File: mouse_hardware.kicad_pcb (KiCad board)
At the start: 4 copper layers, 51 x 82 mm, 48 parts, among them IC1 ADP150AUJZ-2.0-R7, IC2 AP2112K-3.3TRG1, J1 Conn_01x04_Pin, J2 Conn_01x04_Pin, SW1 SW_Push, SW5 SW_Push, U1 STM32F103RETx, U2 PMW3360DM-T2QU, Y1 8MHz

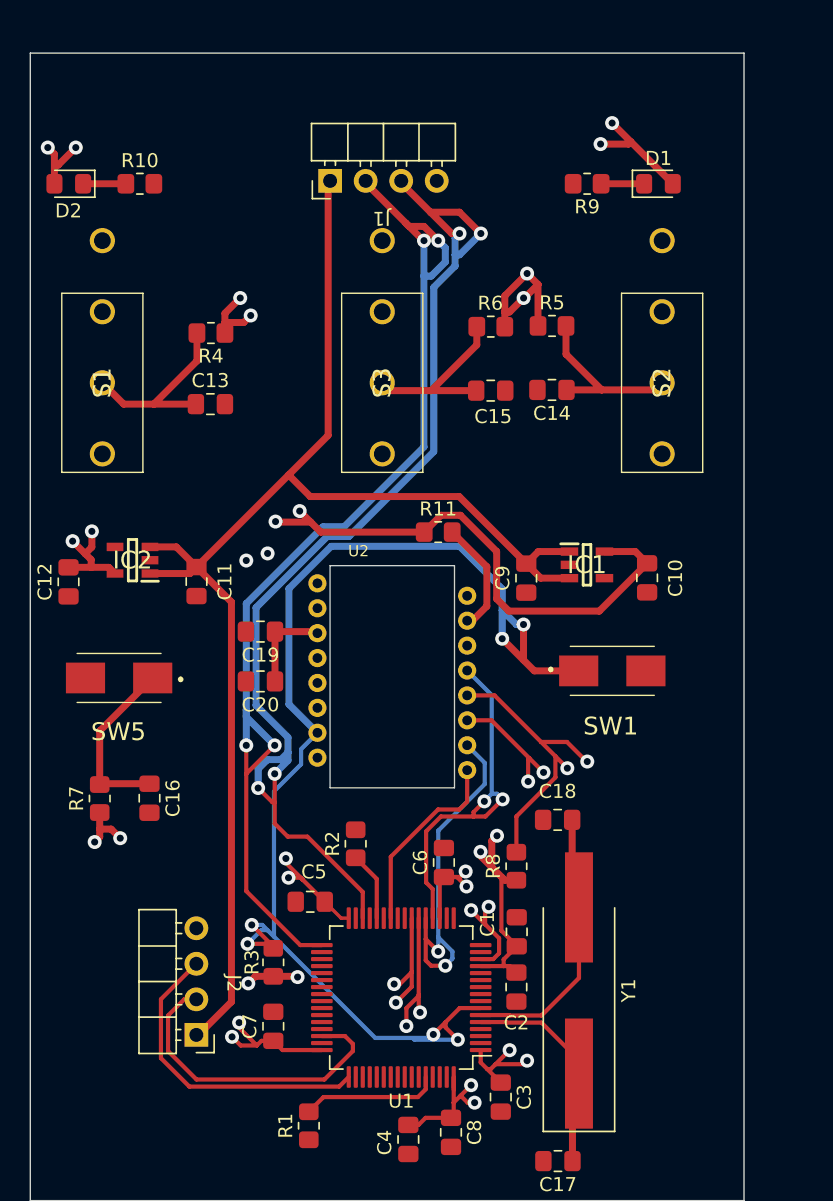
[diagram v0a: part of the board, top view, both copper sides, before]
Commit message: Add connector labels
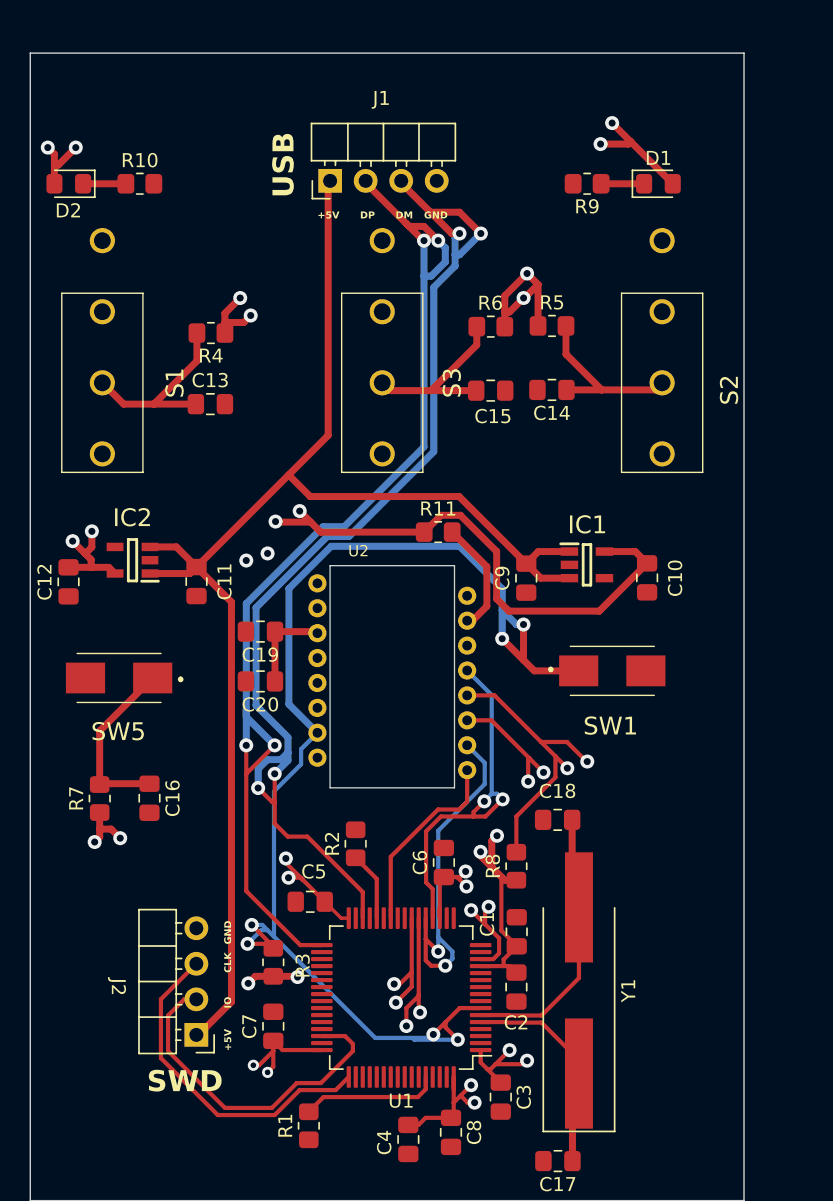
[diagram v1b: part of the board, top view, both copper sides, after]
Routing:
- net SWDIO: track 22.9 -> 24.6 mm
- net SWCLK: track 22.3 -> 24.0 mm
- net +3V3: track 107.5 -> 106.2 mm
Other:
- board text added: "+5V"
- board text added: "CLK"
- board text added: "DM"
- board text added: "DP"
- board text added: "GND"
- board text added: "IO"
- board text added: "SWD"
- board text added: "USB"

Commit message: rev3
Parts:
- moved C7 3.59 mm to (27.9, 84.8), turned to 180 degrees
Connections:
- U1 pad 30: USBDM -> unconnected-(U1-PB11-Pad30)
- U1 pad 33: USBDP -> unconnected-(U1-PB12-Pad33)
- U1 pad 44: unconnected-(U1-PA11-Pad44) -> USBDM
- U1 pad 45: unconnected-(U1-PA12-Pad45) -> USBDP
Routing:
- net USBDP: track 78.5 -> 88.7 mm
- net USBDM: track 78.8 -> 88.6 mm
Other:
- board text added: "IDK MOUSE"
- board text added: "REV3"
